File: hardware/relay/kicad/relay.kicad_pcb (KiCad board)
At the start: 4 copper layers, 70 x 45 mm, 22 parts, among them J1 USB4135-GF-A, SW1 KEY_1, SW10 KEY_9, SW11 KEY_DOT, SW12 KEY_0, SW13 KEY_OK, SW2 KEY_2, SW3 KEY_3, SW4 KEY_CLR, SW5 KEY_4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

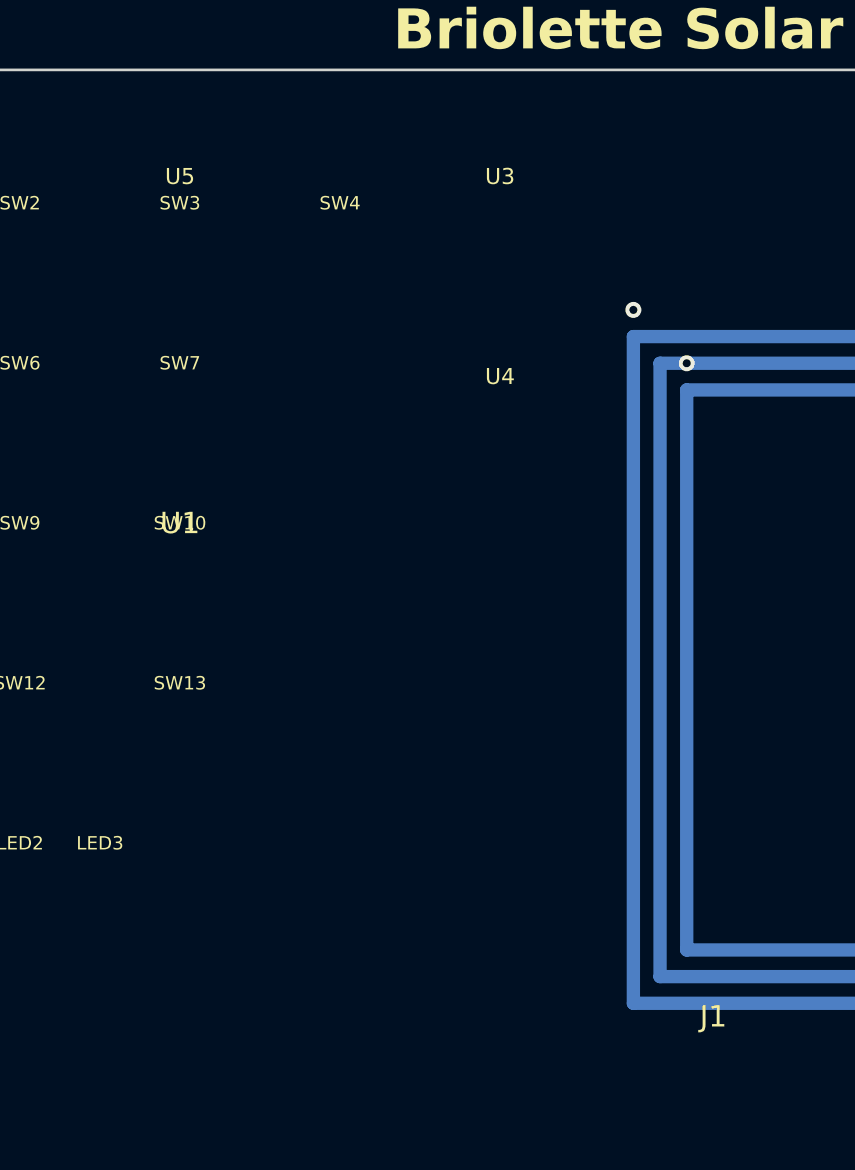
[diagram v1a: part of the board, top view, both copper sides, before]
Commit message: Fix DOA-causing issues in credstick and relay PCB designs
Critical fixes:
- HASL→ENIG copper finish on both PCBs (QFN pads need flat surface)
- Replace stale ATECC608B footprint with Nano-SIM connector on credstick PCB
- Fix NFC antenna spirals: closed rectangles→continuous spiral with crossover vias
- Fix TCA8418/SW3 component overlap at (-20,-15) on relay PCB
- Add missing inter-sheet pins (EPD_BUSY, BTN_L/R, LED, VSCAP_SENSE) to credstick top-level
- Fix button footprints (SW_SPST_PTS810→SW_SPST_3x3mm) to match schematic
- Replace stale I2C nets (SDA/SCL) with SIM interface nets
- Fix nRF52840 package description in both BOMs (aQFN-73 7x7→QFN-48 6x6)
- Remove ATECC608B reference from credstick BOM sourcing guide

https://claude.ai/code/session_01TM1rFxbipYtvAkh4Vt7My7
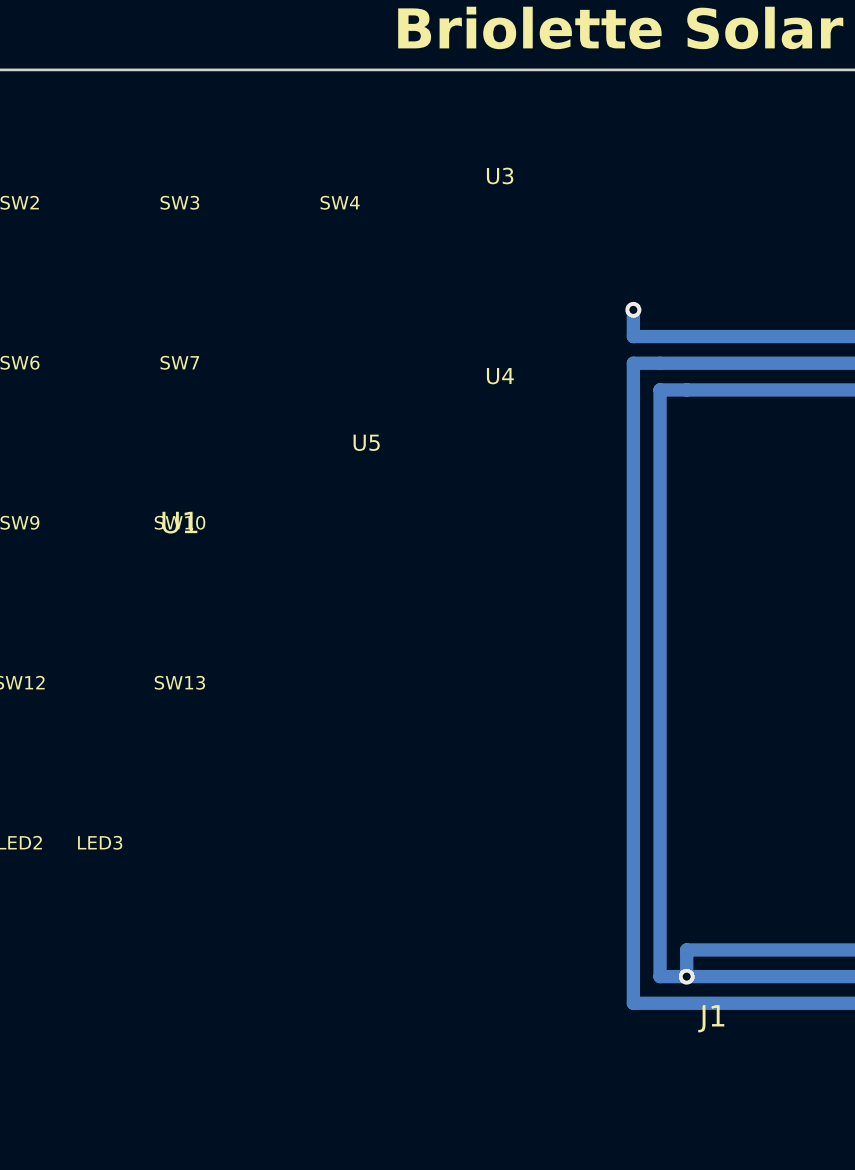
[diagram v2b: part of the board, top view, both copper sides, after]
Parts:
- moved U5 12.2 mm to (-13.0, -5.00)
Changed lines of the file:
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@@
       (layer "dielectric 3" (type "prepreg") (thickness 0.2) (material "FR4") (epsilon_r 4.5))
       (layer "B.Cu" (type "copper") (thickness 0.035))
-      (copper_finish "HASL with lead")
+      (copper_finish "ENIG")
     )
     (pad_to_mask_clearance 0.05)
@@
       (effects (font (size 0.8 0.8) (thickness 0.12))))
   )
-  ;; TCA8418 I2C Keypad Scanner (near MCU)
-  (footprint "relay-lib:WQFN-24-4x4mm" (layer "F.Cu") (at -20.0 -15.0 0)
+  ;; TCA8418 I2C Keypad Scanner (near MCU, between MCU and keypad grid)
+  (footprint "relay-lib:WQFN-24-4x4mm" (layer "F.Cu") (at -13.0 -5.0 0)
     (property "Reference" "U5" (at 0 -3.5 0) (layer "F.SilkS")
       (effects (font (size 0.6 0.6) (thickness 0.1))))
@@
   ;; Generates 13.56 MHz field to power credsticks
   ;; ============================================================
-  ;; Turn 1 (outermost)
-  (gr_line (start -3.0 -12.5) (end 30.0 -12.5)
-    (stroke (width 0.5) (type default)) (layer "B.Cu") (net 19))
-  (gr_line (start 30.0 -12.5) (end 30.0 12.5)
-    (stroke (width 0.5) (type default)) (layer "B.Cu") (net 19))
-  (gr_line (start 30.0 12.5) (end -3.0 12.5)
-    (stroke (width 0.5) (type default)) (layer "B.Cu") (net 19))
-  (gr_line (start -3.0 12.5) (end -3.0 -12.5)
-    (stroke (width 0.5) (type default)) (layer "B.Cu") (net 19))
-  ;; Turn 2
-  (gr_line (start -2.0 -11.5) (end 29.0 -11.5)
-    (stroke (width 0.5) (type default)) (layer "B.Cu") (net 19))
-  (gr_line (start 29.0 -11.5) (end 29.0 11.5)
-    (stroke (width 0.5) (type default)) (layer "B.Cu") (net 19))
-  (gr_line (start 29.0 11.5) (end -2.0 11.5)
-    (stroke (width 0.5) (type default)) (layer "B.Cu") (net 19))
-  (gr_line (start -2.0 11.5) (end -2.0 -11.5)
-    (stroke (width 0.5) (type default)) (layer "B.Cu") (net 19))
-  ;; Turn 3 (innermost)
-  (gr_line (start -1.0 -10.5) (end 28.0 -10.5)
-    (stroke (width 0.5) (type default)) (layer "B.Cu") (net 20))
-  (gr_line (start 28.0 -10.5) (end 28.0 10.5)
-    (stroke (width 0.5) (type default)) (layer "B.Cu") (net 20))
-  (gr_line (start 28.0 10.5) (end -1.0 10.5)
-    (stroke (width 0.5) (type default)) (layer "B.Cu") (net 20))
-  (gr_line (start -1.0 10.5) (end -1.0 -10.5)
-    (stroke (width 0.5) (type default)) (layer "B.Cu") (net 20))
-  ;; NFC antenna vias (connect bottom traces to top-layer PN7150)
+  ;; NFC Reader Antenna: Continuous rectangular spiral, 3 turns
+  ;; Open at left side, each turn steps inward to the next.
+  ;; Trace width: 0.5mm, spacing: 0.5mm, pitch: 1.0mm
+  ;; Start via: F.Cu NFC_TX1 pad to B.Cu
   (via (at -3.0 -13.5) (size 0.6) (drill 0.3)
     (layers "F.Cu" "B.Cu") (net 19))
-  (via (at -1.0 -11.5) (size 0.6) (drill 0.3)
+  ;; Lead-in from via to Turn 1
+  (gr_line (start -3.0 -13.5) (end -3.0 -12.5)
+    (stroke (width 0.5) (type default)) (layer "B.Cu") (net 19))
+  ;; Turn 1 (outermost): top, right, bottom (open at left)
+  (gr_line (start -3.0 -12.5) (end 30.0 -12.5)
+    (stroke (width 0.5) (type default)) (layer "B.Cu") (net 19))
+  (gr_line (start 30.0 -12.5) (end 30.0 12.5)
+    (stroke (width 0.5) (type default)) (layer "B.Cu") (net 19))
+  (gr_line (start 30.0 12.5) (end -3.0 12.5)
+    (stroke (width 0.5) (type default)) (layer "B.Cu") (net 19))
+  ;; Left side stops short — step inward to Turn 2
+  (gr_line (start -3.0 12.5) (end -3.0 -11.5)
+    (stroke (width 0.5) (type default)) (layer "B.Cu") (net 19))
+  (gr_line (start -3.0 -11.5) (end -2.0 -11.5)
+    (stroke (width 0.5) (type default)) (layer "B.Cu") (net 19))
+  ;; Turn 2: top, right, bottom (open at left)
+  (gr_line (start -2.0 -11.5) (end 29.0 -11.5)
+    (stroke (width 0.5) (type default)) (layer "B.Cu") (net 19))
+  (gr_line (start 29.0 -11.5) (end 29.0 11.5)
+    (stroke (width 0.5) (type default)) (layer "B.Cu") (net 19))
+  (gr_line (start 29.0 11.5) (end -2.0 11.5)
+    (stroke (width 0.5) (type default)) (layer "B.Cu") (net 19))
+  ;; Left side stops short — step inward to Turn 3
+  (gr_line (start -2.0 11.5) (end -2.0 -10.5)
+    (stroke (width 0.5) (type default)) (layer "B.Cu") (net 19))
+  (gr_line (start -2.0 -10.5) (end -1.0 -10.5)
+    (stroke (width 0.5) (type default)) (layer "B.Cu") (net 19))
+  ;; Turn 3 (innermost): top, right, half bottom
+  (gr_line (start -1.0 -10.5) (end 28.0 -10.5)
+    (stroke (width 0.5) (type default)) (layer "B.Cu") (net 19))
+  (gr_line (start 28.0 -10.5) (end 28.0 10.5)
+    (stroke (width 0.5) (type default)) (layer "B.Cu") (net 19))
+  (gr_line (start 28.0 10.5) (end -1.0 10.5)
+    (stroke (width 0.5) (type default)) (layer "B.Cu") (net 19))
+  ;; Lead-out from inner end to NFC_TX2 via
+  (gr_line (start -1.0 10.5) (end -1.0 11.5)
+    (stroke (width 0.5) (type default)) (layer "B.Cu") (net 19))
+  ;; End via: inner spiral end crosses to F.Cu for NFC_TX2 connection
+  (via (at -1.0 11.5) (size 0.6) (drill 0.3)
     (layers "F.Cu" "B.Cu") (net 20))
   ;; ============================================================

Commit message: Fix PCB files: convert invalid gr_line+net to segment elements
kicad-cli fails with "Failed to load board" (exit 3) because gr_line
doesn't support the (net N) property in KiCad's S-expression format.
NFC antenna traces on copper layers must use segment elements instead.

Also adds missing UUIDs to vias and zones (required by KiCad 8.0).

https://claude.ai/code/session_019dReYSafgEC1b8rTuLhQSc
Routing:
- net NFC_TX1: track 0.00 -> 305.0 mm
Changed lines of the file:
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@@
     (layers "F.Cu" "B.Cu") (net 19))
   ;; Lead-in from via to Turn 1
-  (gr_line (start -3.0 -13.5) (end -3.0 -12.5)
-    (stroke (width 0.5) (type default)) (layer "B.Cu") (net 19))
+  (segment (start -3.0 -13.5) (end -3.0 -12.5) (width 0.5) (layer "B.Cu") (net 19))
   ;; Turn 1 (outermost): top, right, bottom (open at left)
-  (gr_line (start -3.0 -12.5) (end 30.0 -12.5)
-    (stroke (width 0.5) (type default)) (layer "B.Cu") (net 19))
-  (gr_line (start 30.0 -12.5) (end 30.0 12.5)
-    (stroke (width 0.5) (type default)) (layer "B.Cu") (net 19))
-  (gr_line (start 30.0 12.5) (end -3.0 12.5)
-    (stroke (width 0.5) (type default)) (layer "B.Cu") (net 19))
+  (segment (start -3.0 -12.5) (end 30.0 -12.5) (width 0.5) (layer "B.Cu") (net 19))
+  (segment (start 30.0 -12.5) (end 30.0 12.5) (width 0.5) (layer "B.Cu") (net 19))
+  (segment (start 30.0 12.5) (end -3.0 12.5) (width 0.5) (layer "B.Cu") (net 19))
   ;; Left side stops short — step inward to Turn 2
-  (gr_line (start -3.0 12.5) (end -3.0 -11.5)
-    (stroke (width 0.5) (type default)) (layer "B.Cu") (net 19))
-  (gr_line (start -3.0 -11.5) (end -2.0 -11.5)
-    (stroke (width 0.5) (type default)) (layer "B.Cu") (net 19))
+  (segment (start -3.0 12.5) (end -3.0 -11.5) (width 0.5) (layer "B.Cu") (net 19))
+  (segment (start -3.0 -11.5) (end -2.0 -11.5) (width 0.5) (layer "B.Cu") (net 19))
   ;; Turn 2: top, right, bottom (open at left)
-  (gr_line (start -2.0 -11.5) (end 29.0 -11.5)
-    (stroke (width 0.5) (type default)) (layer "B.Cu") (net 19))
-  (gr_line (start 29.0 -11.5) (end 29.0 11.5)
-    (stroke (width 0.5) (type default)) (layer "B.Cu") (net 19))
-  (gr_line (start 29.0 11.5) (end -2.0 11.5)
-    (stroke (width 0.5) (type default)) (layer "B.Cu") (net 19))
+  (segment (start -2.0 -11.5) (end 29.0 -11.5) (width 0.5) (layer "B.Cu") (net 19))
+  (segment (start 29.0 -11.5) (end 29.0 11.5) (width 0.5) (layer "B.Cu") (net 19))
+  (segment (start 29.0 11.5) (end -2.0 11.5) (width 0.5) (layer "B.Cu") (net 19))
   ;; Left side stops short — step inward to Turn 3
-  (gr_line (start -2.0 11.5) (end -2.0 -10.5)
-    (stroke (width 0.5) (type default)) (layer "B.Cu") (net 19))
-  (gr_line (start -2.0 -10.5) (end -1.0 -10.5)
-    (stroke (width 0.5) (type default)) (layer "B.Cu") (net 19))
+  (segment (start -2.0 11.5) (end -2.0 -10.5) (width 0.5) (layer "B.Cu") (net 19))
+  (segment (start -2.0 -10.5) (end -1.0 -10.5) (width 0.5) (layer "B.Cu") (net 19))
   ;; Turn 3 (innermost): top, right, half bottom
-  (gr_line (start -1.0 -10.5) (end 28.0 -10.5)
-    (stroke (width 0.5) (type default)) (layer "B.Cu") (net 19))
-  (gr_line (start 28.0 -10.5) (end 28.0 10.5)
-    (stroke (width 0.5) (type default)) (layer "B.Cu") (net 19))
-  (gr_line (start 28.0 10.5) (end -1.0 10.5)
-    (stroke (width 0.5) (type default)) (layer "B.Cu") (net 19))
+  (segment (start -1.0 -10.5) (end 28.0 -10.5) (width 0.5) (layer "B.Cu") (net 19))
+  (segment (start 28.0 -10.5) (end 28.0 10.5) (width 0.5) (layer "B.Cu") (net 19))
+  (segment (start 28.0 10.5) (end -1.0 10.5) (width 0.5) (layer "B.Cu") (net 19))
   ;; Lead-out from inner end to NFC_TX2 via
-  (gr_line (start -1.0 10.5) (end -1.0 11.5)
-    (stroke (width 0.5) (type default)) (layer "B.Cu") (net 19))
+  (segment (start -1.0 10.5) (end -1.0 11.5) (width 0.5) (layer "B.Cu") (net 19))
   ;; End via: inner spiral end crosses to F.Cu for NFC_TX2 connection
   (via (at -1.0 11.5) (size 0.6) (drill 0.3)
@@
   ;; GND plane (In1.Cu)
   (zone (net 1) (net_name "GND") (layer "In1.Cu")
-    (uuid "zone-relay-gnd")
     (hatch edge 0.5)
     (connect_pads (clearance 0.3))
@@
   ;; VCC plane (In2.Cu)
   (zone (net 2) (net_name "VCC") (layer "In2.Cu")
-    (uuid "zone-relay-vcc")
     (hatch edge 0.5)
     (connect_pads (clearance 0.3))
@@
   ;; Keep-out under NFC reader antenna (inner layers)
   (zone (net 0) (net_name "") (layer "In1.Cu")
-    (uuid "zone-relay-keepout-gnd")
     (hatch edge 0.5)
     (connect_pads (clearance 0))
@@
     (polygon (pts (xy -5 -14) (xy 32 -14) (xy 32 14) (xy -5 14))))
   (zone (net 0) (net_name "") (layer "In2.Cu")
-    (uuid "zone-relay-keepout-pwr")
     (hatch edge 0.5)
     (connect_pads (clearance 0))
